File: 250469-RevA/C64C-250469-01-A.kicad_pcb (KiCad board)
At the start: 2 copper layers, 390.6 x 136.2 mm, 131 parts, among them J1 Conn_01x20_Male, J10 LED, J2 Conn_02x12_Edge, J3 Conn_02x6_Edge, J4 DIN-6, J5 DIN-8, J6 Conn_02x22_Edge_Female, J7 DIN-7, J8 DB9_Female, J9 DB9_Female, M1 RF_Modulator, Q1 2SD313, Q2 2SC1815, Q3 2SC1815, Q5 2SC1384, U1 6526A, U10 41464, U11 41464, U18 4066, U19 2114, U2 6526A, U20 8701, U21 4066, U22 7416, U23 74LS14, U3 74LS08, U4 23128, U5 2332, U6 8500, U7 8565R2, U8 251715-01, U9 8580R5, Y1 Crystal

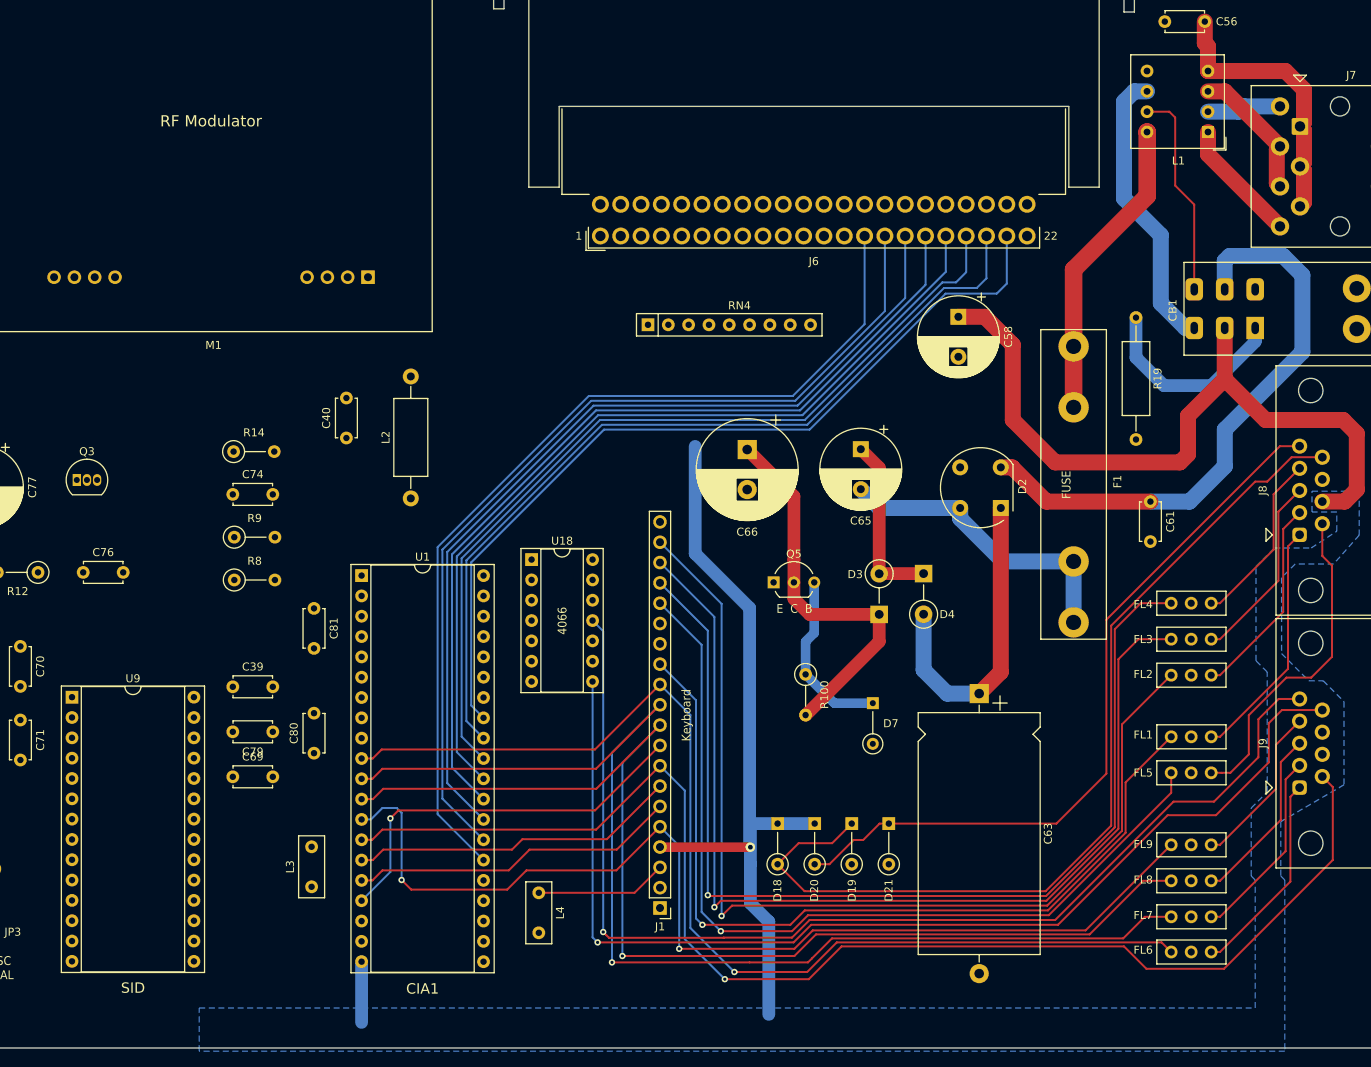
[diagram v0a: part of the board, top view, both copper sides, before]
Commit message: Routed rightmost side of the board
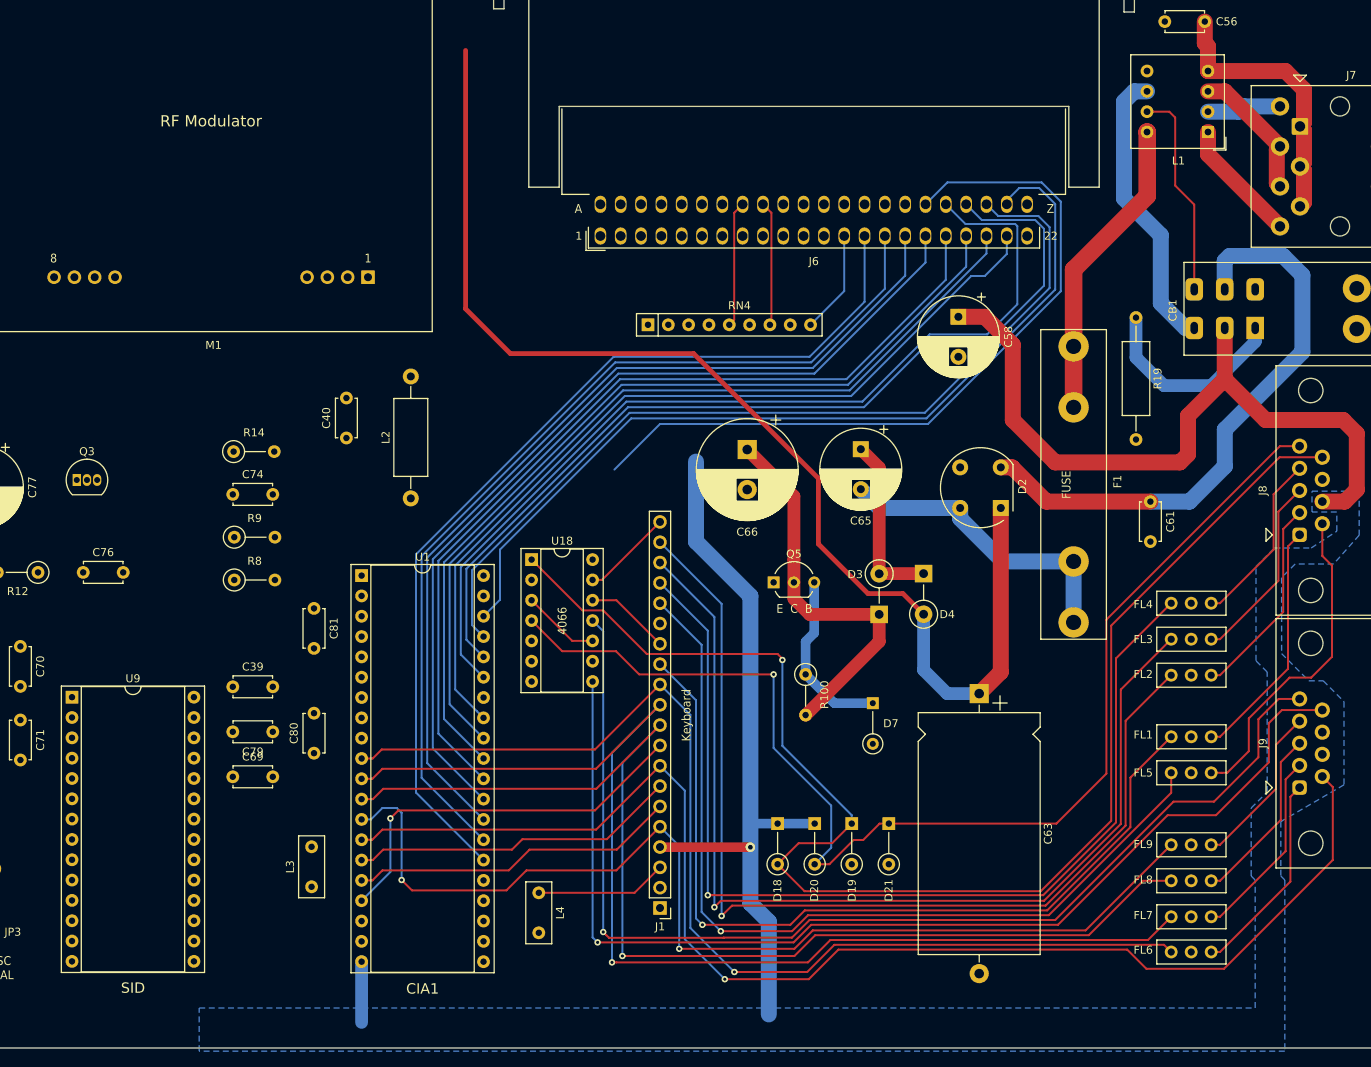
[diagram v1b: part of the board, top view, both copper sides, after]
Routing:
- net A3: track 0.00 -> 117.9 mm
- net A2: track 0.00 -> 116.9 mm
- net A1: track 0.00 -> 112.4 mm
- net A0: track 0.00 -> 110.8 mm
- net +9V_UNREG: track 39.5 -> 149.6 mm
- net A4: track 0.00 -> 95.3 mm
- net /Joystick Ports/POT_BY: track 93.5 -> 154.1 mm, vias 0 -> 1
- net /Joystick Ports/POT_BX: track 118.0 -> 178.3 mm, vias 0 -> 1
- net A13: track 0.00 -> 15.8 mm
- net A12: track 0.00 -> 15.6 mm
- net /CPU - Expansion Port/~DMA: track 0.00 -> 12.8 mm
- net COL7: track 0.00 -> 11.4 mm
- net COL6: track 0.00 -> 10.7 mm
- net POT_Y: track 0.00 -> 9.72 mm
- net +5V: track 195.2 -> 190.9 mm
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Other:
- board text added: "1"
- board text added: "8"
- board text added: "A"
- board text added: "Z"

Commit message: More routing around CIA 1
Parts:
- added REF**: MountingHole_3.7mm, MountingHole:MountingHole_3.7mm, F.Cu at (475.3, 137.5)
- added REF**: MountingHole_3.7mm, MountingHole:MountingHole_3.7mm, F.Cu at (482.4, 138.0)
- added REF**: MountingHole_3.7mm, MountingHole:MountingHole_3.7mm, F.Cu at (485.5, 249.2)
- added REF**: MountingHole_3.7mm, MountingHole:MountingHole_3.7mm, F.Cu at (485.4, 260.8)
- added REF**: MountingHole_2.2mm_M2_Pad, MountingHole:MountingHole_2.2mm_M2_Pad, F.Cu at (457.3, 160.1)
- added REF**: MountingHole_2.2mm_M2_Pad, MountingHole:MountingHole_2.2mm_M2_Pad, F.Cu at (378.4, 160.1)
- moved C58 7.65 mm to (439.4, 181.2), turned to 180 degrees
- moved C66 5.91 mm to (409.6, 196.9), turned to 90 degrees
- moved C40 5.78 mm to (360.0, 195.3)
- moved C80 4.15 mm to (355.8, 224.8)
- moved U9 3.64 mm to (324.1, 218.4)
- moved C81 3.17 mm to (355.7, 207.7)
- moved M1 2.80 mm to (364.7, 168.4)
- moved C39 2.29 mm to (344.8, 218.4)
- moved C69 2.14 mm to (344.8, 229.8)
- moved C79 2.14 mm to (349.8, 224.2)
- moved R100 2.06 mm to (418.6, 220.1)
- moved L2 1.88 mm to (366.2, 195.7)
- moved C56 0.40 mm to (467.1, 137.5)
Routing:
- net /Keyboard - CIA 1/~RESTORE: track 0.00 -> 227.8 mm
- net CNT1: track 0.00 -> 198.5 mm, vias 0 -> 1
- net +9V: track 0.00 -> 172.8 mm, vias 0 -> 2
- net 9V_AC1: track 74.0 -> 243.0 mm, vias 0 -> 2
- net 9V_AC2: track 38.7 -> 191.5 mm, vias 0 -> 2
- net ~INTRES: track 0.00 -> 141.9 mm, vias 0 -> 2
- net PHI2: track 0.00 -> 123.0 mm, vias 0 -> 2
- net SP1: track 0.00 -> 121.9 mm, vias 0 -> 1
- net ~IRQ: track 0.00 -> 115.0 mm
- net R~W: track 0.00 -> 113.7 mm, vias 0 -> 2
- net A4: track 95.3 -> 206.3 mm, vias 0 -> 2
- net POT_X: track 0.00 -> 92.6 mm, vias 0 -> 1
- net A5: track 0.00 -> 79.7 mm
- net A14: track 0.00 -> 78.1 mm
- net A6: track 0.00 -> 76.9 mm
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- added copper zone on B.Cu, net GND
- added copper zone on F.Cu, net GND
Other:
- outline, holes or cut-outs redrawn

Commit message: Changed footprint of DIC connectors and wiring of Color RAM
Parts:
- added REF**: MountingHole_3.7mm, MountingHole:MountingHole_3.7mm, F.Cu at (300.1, 260.7)
- J4: footprint krl_Connector_DIN:CUI-Devices_SDS-60J_DIN-6_Circular -> krl_Connector_DIN:C64_Original_DIN-6_Circular
- J5: footprint krl_Connector_DIN:CUI-Devices_SDS-80J_DIN-8_Circular -> krl_Connector_DIN:C64_Original_DIN-8_Circular
- J7: footprint krl_Connector_DIN:CUI-Devices_SDS-70J_DIN-7_Circular -> krl_Connector_DIN:C64_Original_DIN-7_Circular
- moved U19 12.2 mm to (252.1, 208.1)
- moved J10 11.5 mm to (133.1, 169.5)
- moved R5 10.6 mm to (133.3, 162.6)
- moved RN3 10.5 mm to (161.5, 166.3)
- moved C44 10.2 mm to (116.2, 170.9)
- moved C37 8.62 mm to (293.5, 192.4), turned to 0 degrees
- moved FB2 8.49 mm to (299.4, 156.6)
- moved C76 8.21 mm to (334.4, 204.1), turned to 180 degrees
- moved FB4 7.96 mm to (291.8, 156.6)
- moved U2 7.68 mm to (105.2, 188.5)
- moved U23 7.65 mm to (135.9, 176.8)
- moved C35 7.51 mm to (293.1, 246.6)
- moved R16 7.13 mm to (124.1, 174.4)
- moved D6 7.13 mm to (129.3, 174.1)
- moved C55 6.77 mm to (249.0, 194.2)
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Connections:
- U19 pad 1: A6 -> A9
- U19 pad 15: A9 -> A4
- U19 pad 16: A8 -> A6
- U19 pad 17: A7 -> A8
- U19 pad 2: A5 -> A7
- U19 pad 3: A4 -> A5
- U19 pad 5: A0 -> A2
- U19 pad 7: A2 -> A0
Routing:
- net SP1: track 121.9 -> 359.8 mm, vias 1 -> 2
- net A8: track 73.8 -> 290.8 mm, vias 0 -> 3
- net TOD: track 0.00 -> 215.7 mm, vias 0 -> 2
- net +5V: track 245.0 -> 459.2 mm, vias 5 -> 6
- net A11: track 65.5 -> 266.5 mm, vias 0 -> 3
- net A9: track 71.0 -> 271.2 mm, vias 0 -> 3
- net A10: track 68.2 -> 248.3 mm, vias 0 -> 3
- net CNT1: track 198.5 -> 359.0 mm, vias 1 -> 2
- net ~CIA1: track 0.00 -> 156.5 mm, vias 0 -> 2
- net A4: track 206.3 -> 361.6 mm
- net ~IRQ: track 115.0 -> 270.3 mm, vias 0 -> 1
- net R~W: track 113.7 -> 253.6 mm, vias 2 -> 4
- net ~SID: track 0.00 -> 125.5 mm, vias 0 -> 2
- net A6: track 76.9 -> 201.4 mm, vias 0 -> 1
- net AUDIO_IN: track 0.00 -> 124.5 mm, vias 0 -> 2
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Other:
- outline, holes or cut-outs redrawn

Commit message: More routing around the memory controller
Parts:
- moved R101 4.94 mm to (217.2, 229.4)
- moved JP3 3.75 mm to (309.6, 246.5)
- moved C94 2.95 mm to (252.7, 151.0)
- moved C70 2.81 mm to (318.9, 218.4)
- moved C71 2.81 mm to (318.9, 227.6)
- moved C1 2.65 mm to (230.1, 146.9)
- moved Y1 2.22 mm to (306.8, 231.0)
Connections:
- CB1 pad : (no net) -> GND
- J3 pad B: (no net) -> +5V
- J4 pad 0: (no net) -> GND
- J5 pad 0: (no net) -> GND
- J7 pad 0: (no net) -> GND
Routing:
- net +5V: track 459.2 -> 800.3 mm, vias 6 -> 14
- net PHI2: track 241.7 -> 381.2 mm, vias 4 -> 6
- net MA4: track 20.9 -> 139.3 mm, vias 0 -> 2
- net MA5: track 23.7 -> 139.3 mm, vias 0 -> 1
- net MA3: track 18.1 -> 132.6 mm, vias 0 -> 2
- net MA1: track 12.5 -> 125.0 mm, vias 0 -> 1
- net MA2: track 15.3 -> 127.3 mm, vias 0 -> 2
- net MA0: track 9.76 -> 121.7 mm, vias 0 -> 1
- net A3: track 261.7 -> 357.2 mm, vias 2 -> 4
- net A2: track 265.7 -> 356.6 mm, vias 2 -> 4
- net ~INTRES: track 197.3 -> 287.4 mm, vias 3 -> 5
- net /Video - ClockGen/SL: track 61.1 -> 151.3 mm, vias 0 -> 3
- net A0: track 266.1 -> 352.7 mm, vias 2 -> 4
- net /Video - ClockGen/COLOR: track 60.1 -> 146.2 mm, vias 0 -> 3
- net /Memory Controller - RAM/~WE: track 0.00 -> 85.1 mm, vias 0 -> 2
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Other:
- board text added: "251715-01"
- board text added: "6526A"
- board text added: "8500"
- board text added: "Audio/Video"
- board text added: "Serial port"

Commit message: More routing
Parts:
- moved C55 0.95 mm to (249.9, 194.5)
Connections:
- J3 pad D: (no net) -> ~SRQ
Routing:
- net A7: track 197.9 -> 421.8 mm, vias 1 -> 3
- net A6: track 201.4 -> 420.5 mm, vias 1 -> 2
- net A5: track 200.1 -> 417.0 mm, vias 1 -> 2
- net A10: track 248.3 -> 437.6 mm, vias 3 -> 4
- net A11: track 280.1 -> 458.6 mm, vias 3 -> 5
- net R~W: track 253.6 -> 389.7 mm, vias 4 -> 5
- net A8: track 290.9 -> 422.5 mm
- net A12: track 243.2 -> 361.8 mm, vias 2 -> 3
- net A3: track 357.2 -> 464.4 mm
- net A9: track 306.8 -> 411.6 mm
- net A4: track 361.4 -> 466.0 mm
- net A2: track 356.6 -> 460.3 mm
- net A1: track 344.6 -> 448.3 mm
- net A0: track 352.7 -> 456.4 mm
- net AEC: track 31.7 -> 130.6 mm, vias 0 -> 3
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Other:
- board text added: "NC"

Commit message: Initial port to v7
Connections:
- net /CPU - Expansion Port/~DMA renamed /CPU - Expansion Port/~{DMA}
- net /Keyboard - CIA 1/~RESTORE renamed /Keyboard - CIA 1/~{RESTORE}
- net /Memory Controller - RAM/~CASR renamed /Memory Controller - RAM/~{CASR}
- net /Memory Controller - RAM/~COLRAM renamed /Memory Controller - RAM/~{COLRAM}
- net /Memory Controller - RAM/~WE renamed /Memory Controller - RAM/~{WE}
- net /User Port - CIA 2/~FLAG_2 renamed /User Port - CIA 2/~{FLAG_2}
- net /User Port - CIA 2/~PC2 renamed /User Port - CIA 2/~{PC2}
- net R~W renamed R~{W}
- net ~CAS renamed ~{CAS}
- net ~CHAREN renamed ~{CHAREN}
- net ~CHAROM renamed ~{CHAROM}
- net ~CIA1 renamed ~{CIA1}
- net ~CIA2 renamed ~{CIA2}
- net ~EXROM renamed ~{EXROM}
- net ~EXTRST renamed ~{EXTRST}
- net ~GAME renamed ~{GAME}
- net ~HIRAM renamed ~{HIRAM}
- net ~INTRES renamed ~{INTRES}
- net ~IO1 renamed ~{IO1}
- net ~IO2 renamed ~{IO2}
- net ~IRQ renamed ~{IRQ}
- net ~KBR_CS renamed ~{KBR_CS}
- net ~LORAM renamed ~{LORAM}
- net ~NMI renamed ~{NMI}
- net ~RAS renamed ~{RAS}
- net ~ROMH renamed ~{ROMH}
- net ~ROML renamed ~{ROML}
- net ~SID renamed ~{SID}
- net ~SRQ renamed ~{SRQ}
- net ~VA14 renamed ~{VA14}
- net ~VA15 renamed ~{VA15}
- net ~VIC renamed ~{VIC}
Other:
- net class Default removed
